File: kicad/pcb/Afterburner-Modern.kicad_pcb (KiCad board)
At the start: 2 copper layers, 0.1 x 0.1 mm, 0 parts

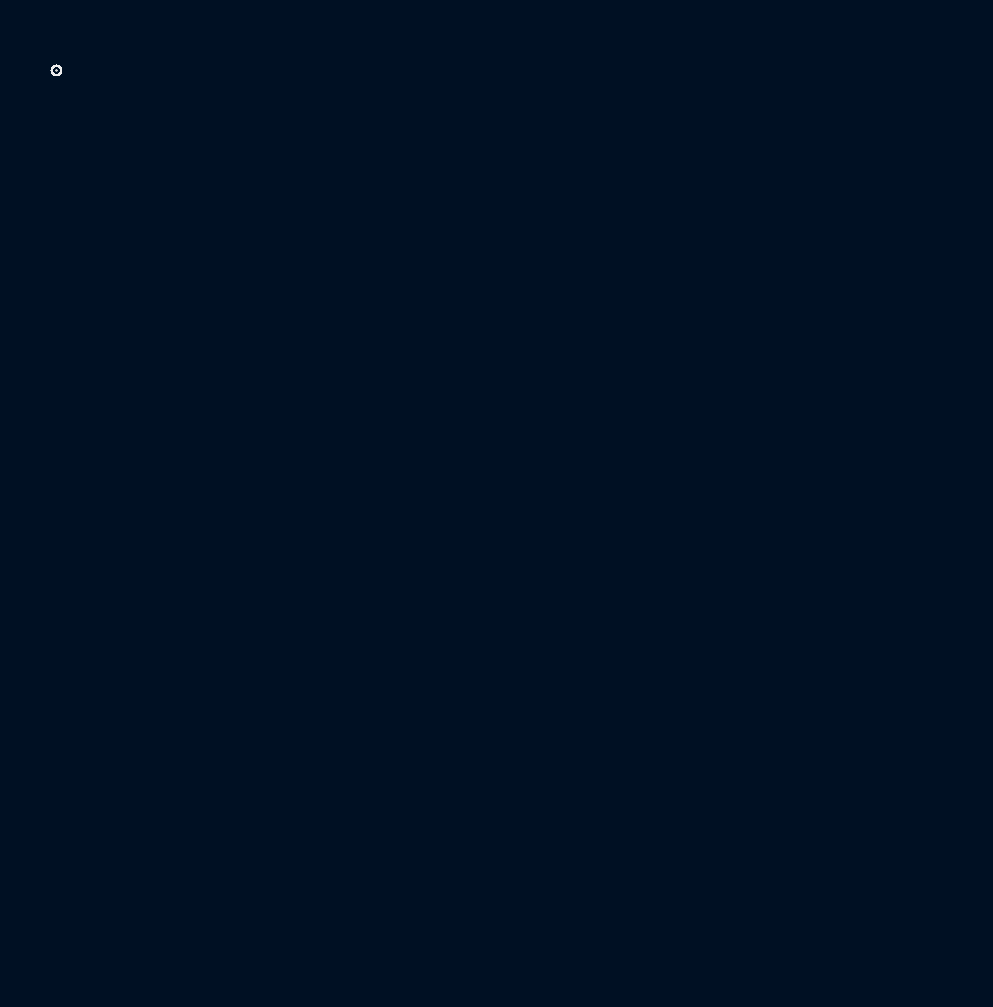
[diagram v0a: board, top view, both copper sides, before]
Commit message: kicad: Complete PCB layout redesign with zone-based placement
- Rewrite plan.py: zone-based layout (power, MCU, display, sensors, I/O,
  external sensors, expansion) with proper spacing between IC rows
- Fix apply.py: integer coordinate formatting to match KiCad file format
- Update critical.py: all route coordinates match new component positions
- Add autoroute_full.py: pipeline script for autorouting from placed board
- Fix freerouting path: use external/freerouting-2.2.4-linux-x64/bin/freerouting
  instead of system install
- Move switches to left edge (SW1 at 10,23; SW2 at 16,23)
- Group display+touch adjacent (both at x=48) for FPC cable routing
- Group sensors together (U4, U7 at x=62) for clean I2C routing
- 0 DRC violations, fabrication files exported
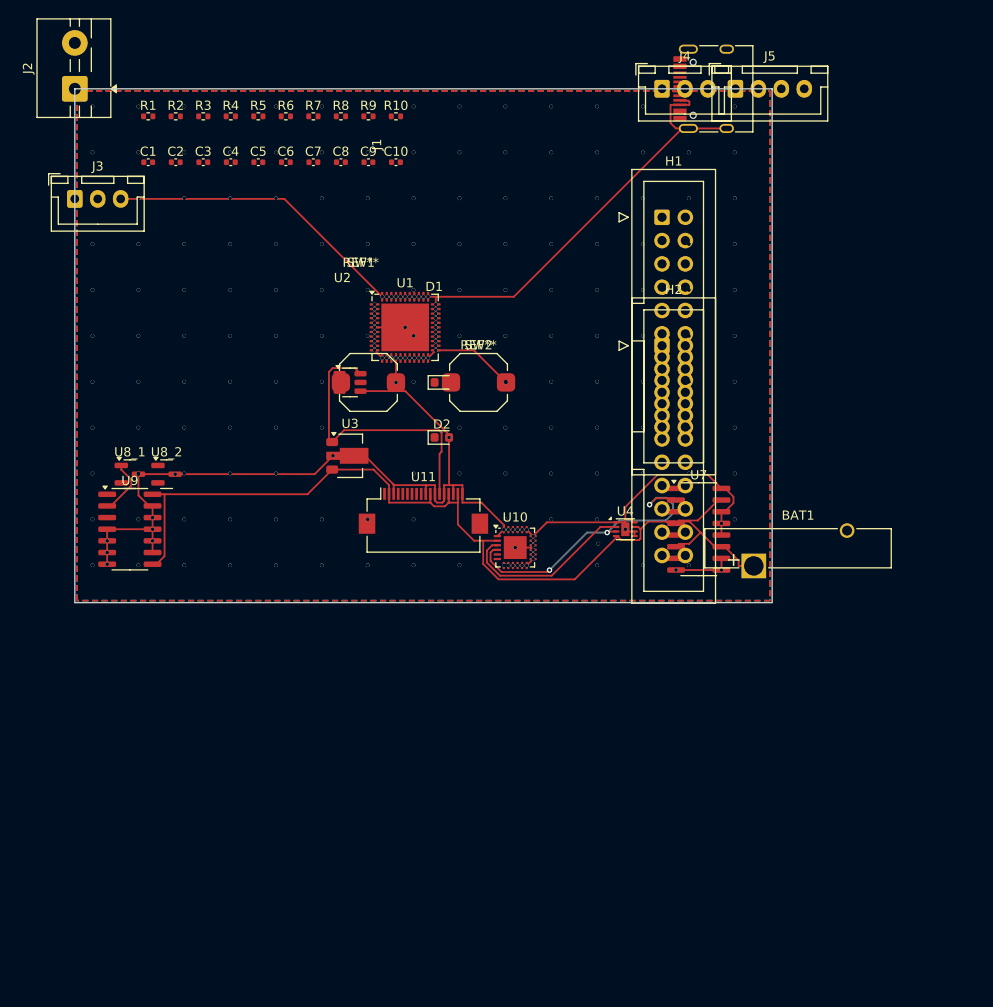
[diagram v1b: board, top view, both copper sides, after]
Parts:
- added BAT1: Battery_Panasonic_CR2032-VS1N_Vertical_CircularHoles, Battery_Panasonic_CR2032-VS1N_Vertical_CircularHoles, F.Cu at (76.0, 54.0)
- added C1: C_0402_1005Metric, C_0402_1005Metric, F.Cu at (10.0, 10.0)
- added C10: C_0402_1005Metric, C_0402_1005Metric, F.Cu at (37.0, 10.0)
- added C2: C_0402_1005Metric, C_0402_1005Metric, F.Cu at (13.0, 10.0)
- added C3: C_0402_1005Metric, C_0402_1005Metric, F.Cu at (16.0, 10.0)
- added C4: C_0402_1005Metric, C_0402_1005Metric, F.Cu at (19.0, 10.0)
- added C5: C_0402_1005Metric, C_0402_1005Metric, F.Cu at (22.0, 10.0)
- added C6: C_0402_1005Metric, C_0402_1005Metric, F.Cu at (25.0, 10.0)
- added C7: C_0402_1005Metric, C_0402_1005Metric, F.Cu at (28.0, 10.0)
- added C8: C_0402_1005Metric, C_0402_1005Metric, F.Cu at (31.0, 10.0)
- added C9: C_0402_1005Metric, C_0402_1005Metric, F.Cu at (34.0, 10.0)
- added D1: LED_0603_1608Metric, LED_0603_1608Metric, F.Cu at (42.0, 34.0)
- added D2: LED_0603_1608Metric, LED_0603_1608Metric, F.Cu at (42.0, 40.0)
- added H1: IDC-Header_2x10_P2.54mm_Vertical, IDC-Header_2x10_P2.54mm_Vertical, F.Cu at (66.0, 16.0)
- added H2: IDC-Header_2x10_P2.54mm_Vertical, IDC-Header_2x10_P2.54mm_Vertical, F.Cu at (66.0, 30.0)
- added J1: USB_C_Receptacle_HRO_TYPE-C-31-M-12, USB_C_Receptacle_HRO_TYPE-C-31-M-12, B.Cu at (72.0, 2.00)
- added J2: TerminalBlock_MaiXu_MX126-5.0-02P_1x02_P5.00mm, TerminalBlock_MaiXu_MX126-5.0-02P_1x02_P5.00mm, B.Cu at (2.00, 2.00)
- added J3: JST_XH_B3B-XH-A_1x03_P2.50mm_Vertical, JST_XH_B3B-XH-A_1x03_P2.50mm_Vertical, F.Cu at (2.00, 14.0)
- added J4: JST_XH_B3B-XH-A_1x03_P2.50mm_Vertical, JST_XH_B3B-XH-A_1x03_P2.50mm_Vertical, F.Cu at (66.0, 2.00)
- added J5: JST_XH_B4B-XH-A_1x04_P2.50mm_Vertical, JST_XH_B4B-XH-A_1x04_P2.50mm_Vertical, F.Cu at (74.0, 2.00)
- added R1: R_0402_1005Metric, R_0402_1005Metric, F.Cu at (10.0, 5.00)
- added R10: R_0402_1005Metric, R_0402_1005Metric, F.Cu at (37.0, 5.00)
- added R2: R_0402_1005Metric, R_0402_1005Metric, F.Cu at (13.0, 5.00)
- added R3: R_0402_1005Metric, R_0402_1005Metric, F.Cu at (16.0, 5.00)
- added R4: R_0402_1005Metric, R_0402_1005Metric, F.Cu at (19.0, 5.00)
- added R5: R_0402_1005Metric, R_0402_1005Metric, F.Cu at (22.0, 5.00)
- added R6: R_0402_1005Metric, R_0402_1005Metric, F.Cu at (25.0, 5.00)
- added R7: R_0402_1005Metric, R_0402_1005Metric, F.Cu at (28.0, 5.00)
- added R8: R_0402_1005Metric, R_0402_1005Metric, F.Cu at (31.0, 5.00)
- added R9: R_0402_1005Metric, R_0402_1005Metric, F.Cu at (34.0, 5.00)
- added SW1: SW_Push_1TS009xxxx-xxxx-xxxx_6x6x5mm, SW_Push_1TS009xxxx-xxxx-xxxx_6x6x5mm, F.Cu at (34.0, 34.0)
- added SW2: SW_Push_1TS009xxxx-xxxx-xxxx_6x6x5mm, SW_Push_1TS009xxxx-xxxx-xxxx_6x6x5mm, F.Cu at (46.0, 34.0)
- added U1: QFN-44-1EP_7x7mm_P0.5mm_EP5.2x5.2mm, QFN-44-1EP_7x7mm_P0.5mm_EP5.2x5.2mm, F.Cu at (38.0, 28.0)
- added U10: QFN-24-1EP_4x4mm_P0.5mm_EP2.5x2.5mm, QFN-24-1EP_4x4mm_P0.5mm_EP2.5x2.5mm, F.Cu at (50.0, 52.0)
- added U11: Hirose_FH12-18S-0.5SH_1x18-1MP_P0.50mm_Horizontal, Hirose_FH12-18S-0.5SH_1x18-1MP_P0.50mm_Horizontal, F.Cu at (40.0, 48.0)
- added U2: SOT-23-6, SOT-23-6, F.Cu at (32.0, 34.0)
- added U3: SOT-89-3, SOT-89-3, F.Cu at (32.0, 42.0)
- added U4: DFN-8-1EP_2x2mm_P0.5mm_EP0.9x1.5mm, DFN-8-1EP_2x2mm_P0.5mm_EP0.9x1.5mm, F.Cu at (62.0, 50.0)
- added U7: SOIC-16_3.9x9.9mm_P1.27mm, SOIC-16_3.9x9.9mm_P1.27mm, F.Cu at (70.0, 50.0)
- added U8_1: SOT-23, SOT-23, F.Cu at (8.00, 44.0)
- added U8_2: SOT-23, SOT-23, F.Cu at (12.0, 44.0)
- added U9: SOIC-14_3.9x8.7mm_P1.27mm, SOIC-14_3.9x8.7mm_P1.27mm, F.Cu at (8.00, 50.0)
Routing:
- net GND: track 0.00 -> 260.0 mm, vias 0 -> 236
- net 3V3: track 0.00 -> 106.0 mm
- net I2C_SCL: track 0.00 -> 33.2 mm, vias 0 -> 3
- net 5V: track 0.00 -> 31.0 mm
- net I2C_SDA: track 0.00 -> 19.6 mm
- net BLUE_TX_OUT: track 0.00 -> 6.19 mm
- net (no net): vias 48 -> 0
- added copper zone on B.Cu, net GND
- added copper zone on F.Cu, net GND
- removed copper zone on B.Cu, net (none)
- removed copper zone on F.Cu, net (none)
- removed copper zone on F.Cu, net 0
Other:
- board size 0.1 x 0.1 mm -> 76 x 56 mm

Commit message: Fix PCB DRC violations: increase board to 100mm, remove display mount holes, re-space components
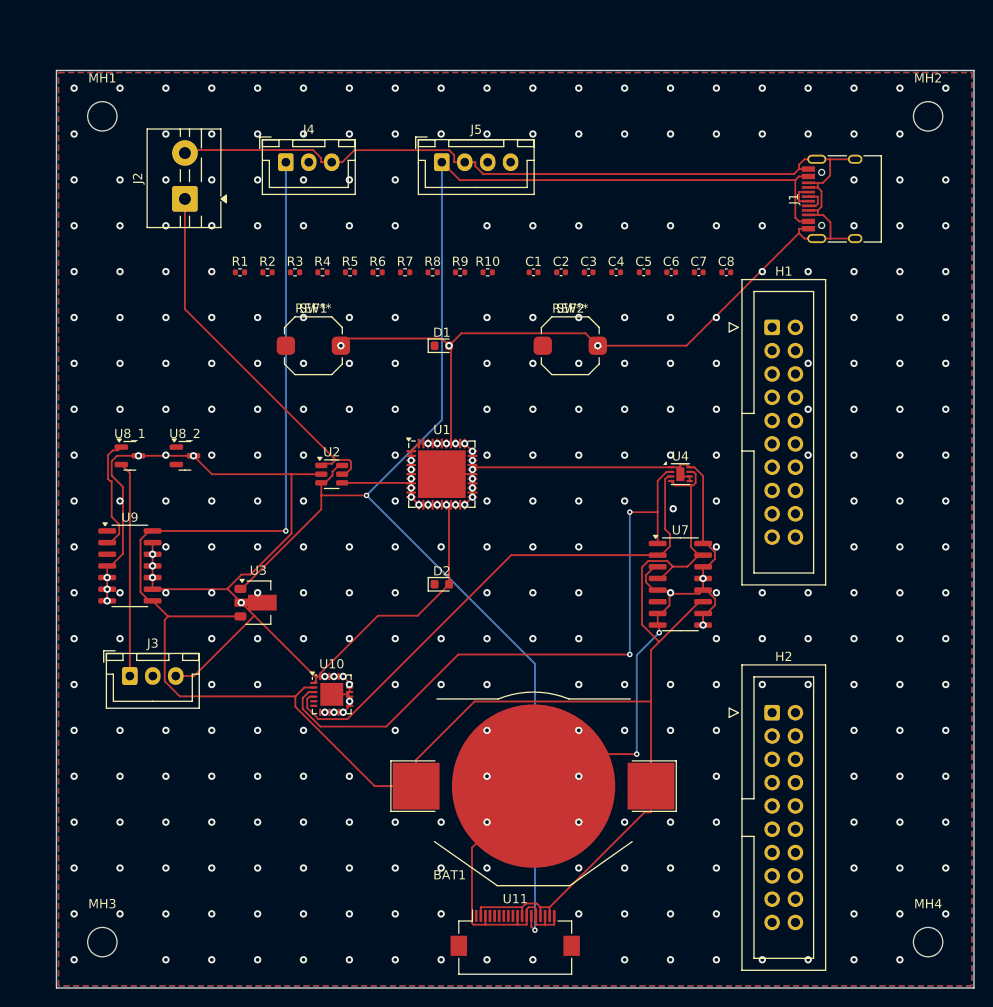
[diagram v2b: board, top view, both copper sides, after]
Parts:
- removed C10, C9: C_0402_1005Metric, C_0402_1005Metric
- added MH1: MountingHole_3.2mm_M3, MountingHole_3.2mm_M3, F.Cu at (5.00, 5.00)
- added MH2: MountingHole_3.2mm_M3, MountingHole_3.2mm_M3, F.Cu at (95.0, 5.00)
- added MH3: MountingHole_3.2mm_M3, MountingHole_3.2mm_M3, F.Cu at (5.00, 95.0)
- added MH4: MountingHole_3.2mm_M3, MountingHole_3.2mm_M3, F.Cu at (95.0, 95.0)
- BAT1: value Battery_Panasonic_CR2032-VS1N_Vertical_CircularHoles -> BatteryHolder_Keystone_3002_1x2032; footprint Battery_Panasonic_CR2032-VS1N_Vertical_CircularHoles -> BatteryHolder_Keystone_3002_1x2032
- H1, H2: moved to B.Cu
- moved J3 52.3 mm to (8.00, 66.0)
- moved U11 47.1 mm to (50.0, 94.0)
- moved C1 43.7 mm to (52.0, 22.0)
- moved C2 43.7 mm to (55.0, 22.0)
- moved C3 43.7 mm to (58.0, 22.0)
- moved C4 43.7 mm to (61.0, 22.0)
- moved C5 43.7 mm to (64.0, 22.0)
- moved C6 43.7 mm to (67.0, 22.0)
- moved C7 43.7 mm to (70.0, 22.0)
- moved C8 43.7 mm to (73.0, 22.0)
- moved J4 41.8 mm to (25.0, 10.0)
- moved H2 41.8 mm to (78.0, 70.0)
- moved BAT1 33.9 mm to (52.0, 78.0)
- moved J5 33.0 mm to (42.0, 10.0)
- moved U10 25.6 mm to (30.0, 68.0)
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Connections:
- J1 pad A1: USB_D- -> GND
- J1 pad A4: USB_D+ -> 5V
- J1 pad A6: GND -> USB_D+
- J1 pad A7: GND -> USB_D-
- J1 pad B1: USB_D+ -> GND
- J1 pad B4: USB_D- -> 5V
- J1 pad B6: GND -> USB_D+
- J1 pad B7: GND -> USB_D-
- U7 pad 6: 3V3 -> (no net)
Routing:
- net GND: track 260.0 -> 461.3 mm, vias 236 -> 367
- net 5V: track 31.0 -> 166.6 mm, vias 0 -> 2
- net 3V3: track 106.0 -> 231.7 mm, vias 0 -> 1
- net I2C_SDA: track 19.6 -> 69.6 mm, vias 0 -> 2
- net 12V: track 0.00 -> 40.8 mm
- net I2C_SCL: track 33.2 -> 58.0 mm, vias 3 -> 0
- net BLUE_TX_H: track 0.00 -> 23.4 mm
- net BLUE_TX_OUT: track 6.19 -> 12.7 mm
- net USB_D+: track 0.00 -> 3.05 mm
- net USB_D-: track 0.00 -> 2.92 mm
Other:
- board size 76 x 56 mm -> 100 x 100 mm
